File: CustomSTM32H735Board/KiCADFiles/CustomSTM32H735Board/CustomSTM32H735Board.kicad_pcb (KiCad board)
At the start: 2 copper layers, 4 parts, among them U1 STM32H735IGKx, U2 STM32H735IGTx

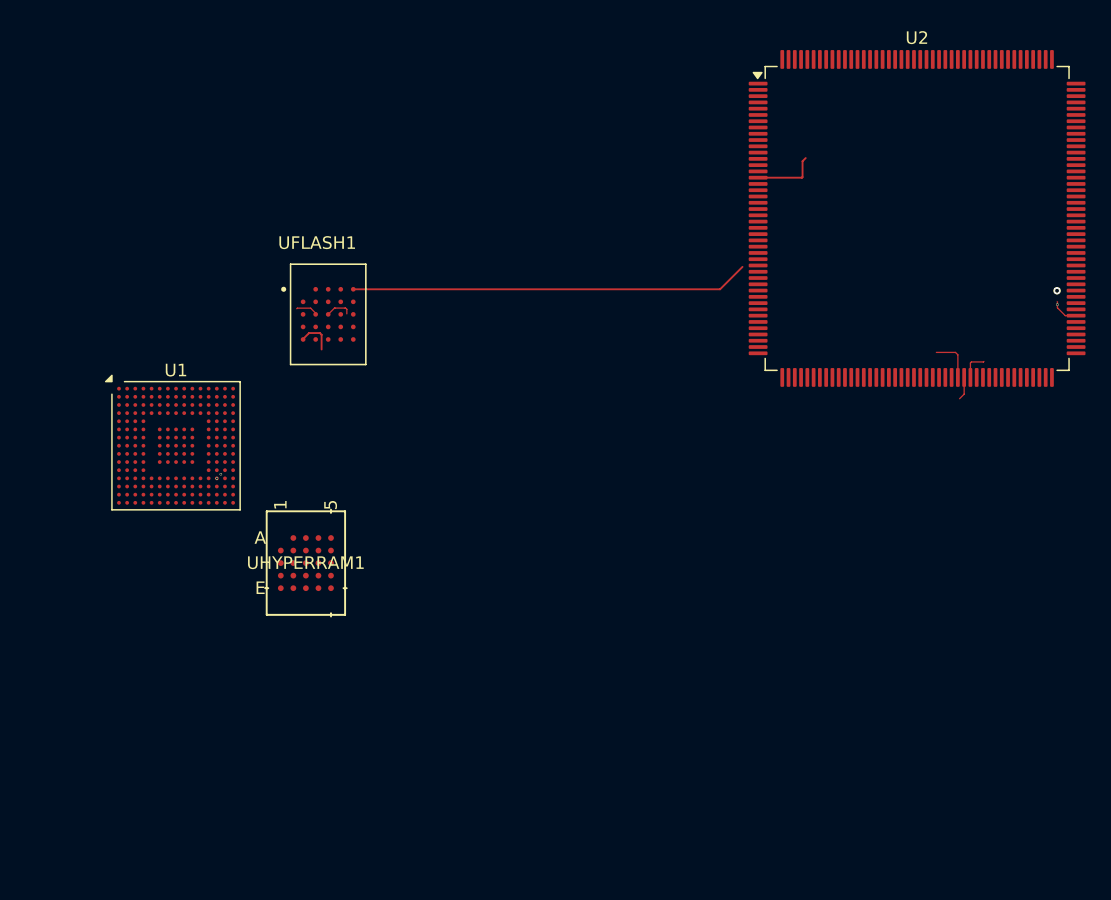
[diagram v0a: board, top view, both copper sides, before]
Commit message: started to assign LCD connector to STM32H735. Added NRST and Boot0 switch.
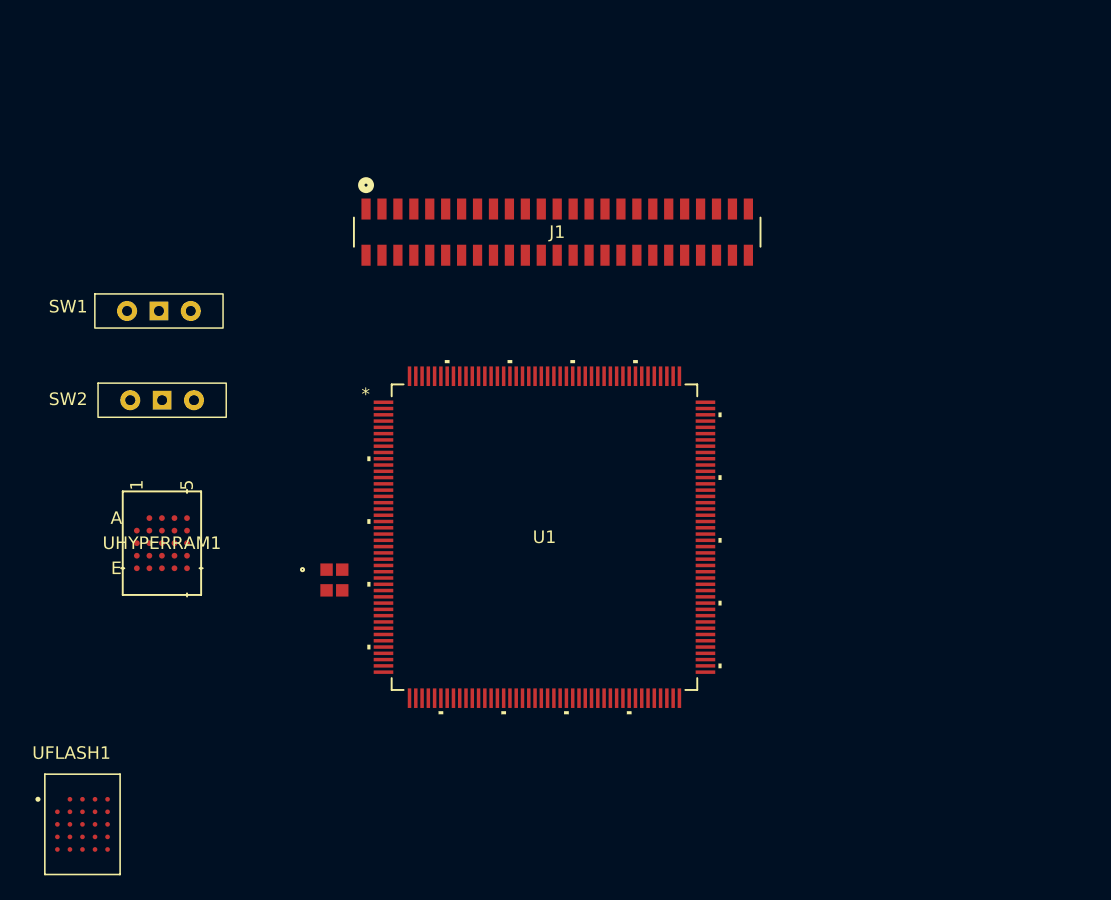
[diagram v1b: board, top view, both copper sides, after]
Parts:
- removed U2: STM32H735IGTx, Package_QFP:LQFP-176_24x24mm_P0.5mm
- added J1: FLE-125-01-G-DV, Private:CON50_2X25_UF_FLE_SAI, F.Cu at (125.5, 57.0)
- added SW1: SW_Wuerth_450301014042, Button_Switch_THT:SW_Slide-03_Wuerth-WS-SLTV_10x2.5x6.4_P2.54mm, F.Cu at (109.0, 61.5)
- added SW2: SW_Wuerth_450301014042, Button_Switch_THT:SW_Slide-03_Wuerth-WS-SLTV_10x2.5x6.4_P2.54mm, F.Cu at (109.2, 68.6)
- added X1: NSC5004A-25M, Private:NSC5004_NDK, F.Cu at (123.0, 82.9)
- U1: value STM32H735IGKx -> STM32H735IGT6; footprint Package_BGA:UFBGA-201_10x10mm_Layout15x15_P0.65mm -> Private:LQFP176_STM32H735IGT6_STM-M
- moved UFLASH1 45.1 mm to (102.9, 102.4)
- moved U1 30.3 mm to (139.7, 79.5)
- moved UHYPERRAM1 11.6 mm to (109.2, 80.0)
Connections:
- UFLASH1 pad B2: /PF10 -> /PB2
- UFLASH1 pad C3: /PB2 -> /PC5
- UFLASH1 pad D2: /PD12 -> /PF9
- UFLASH1 pad D3: /PD11 -> /PF8
- UFLASH1 pad D4: /PD13 -> /PA6
- UFLASH1 pad D5: /PD4 -> /PE7
- UFLASH1 pad E1: /PD7 -> /PE10
- UFLASH1 pad E2: /PG9 -> /PC3_C
- UFLASH1 pad E3: /PD5 -> /PC2_C
- UHYPERRAM1 pad B4: Net-(UHYPERRAM1-VCC) -> +3.3V
- UHYPERRAM1 pad D1: Net-(UHYPERRAM1-VCC) -> +3.3V
- UHYPERRAM1 pad E4: Net-(UHYPERRAM1-VCC) -> +3.3V
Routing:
- net /PG6: track 33.6 -> 0.00 mm
- net unconnected-(U2-VDDSMPS-Pad16): track 5.19 -> 0.00 mm
- net unconnected-(U2-PE11-Pad73): track 3.60 -> 0.00 mm
- net /PD7: track 2.94 -> 0.00 mm
- net unconnected-(U2-PD12-Pad95): track 2.47 -> 0.00 mm, vias 2 -> 0
- net unconnected-(U2-PE13-Pad75): track 2.28 -> 0.00 mm
- net /PB2: track 2.11 -> 0.00 mm
- net unconnected-(U2-PE12-Pad74): track 1.85 -> 0.00 mm
- net unconnected-(U1-PH11-PadM13): vias 1 -> 0
- net (no net): vias 2 -> 0

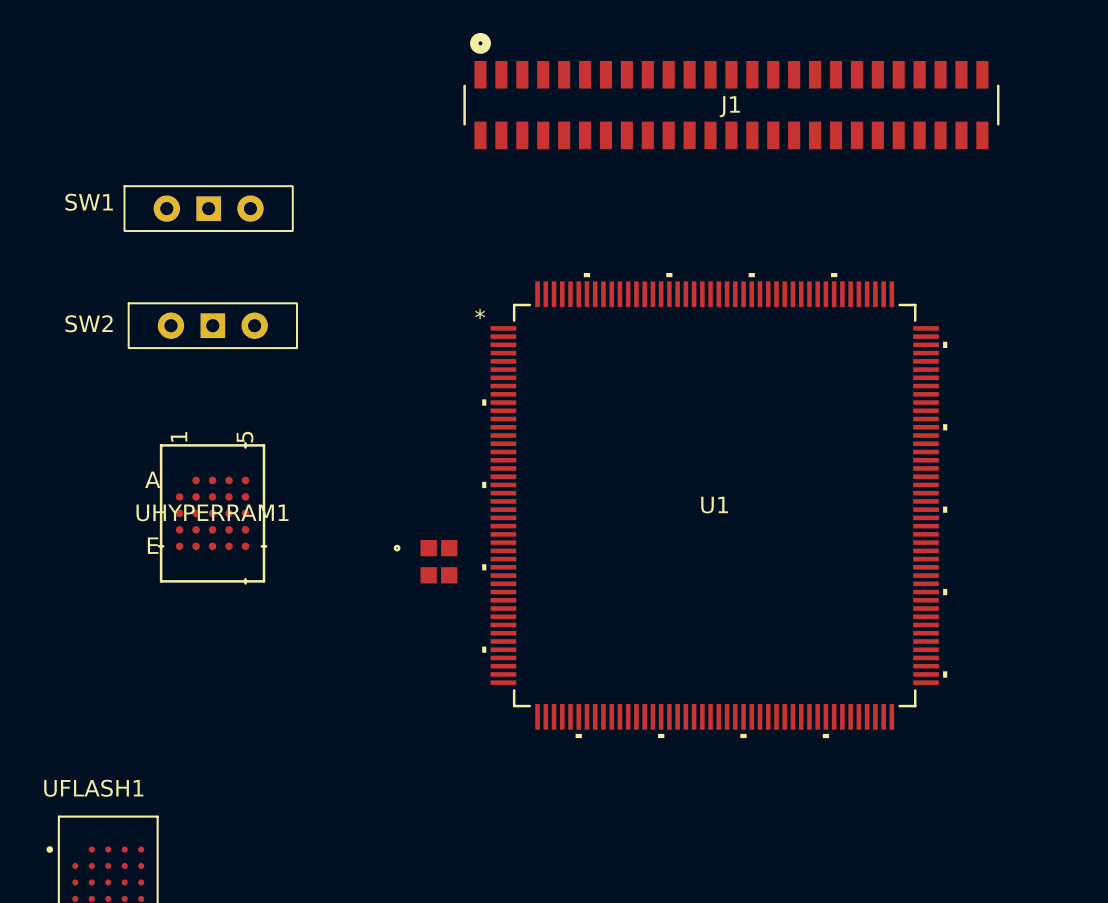
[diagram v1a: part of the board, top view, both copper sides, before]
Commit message: cleaned up repo by eliminating double STM32-DK files
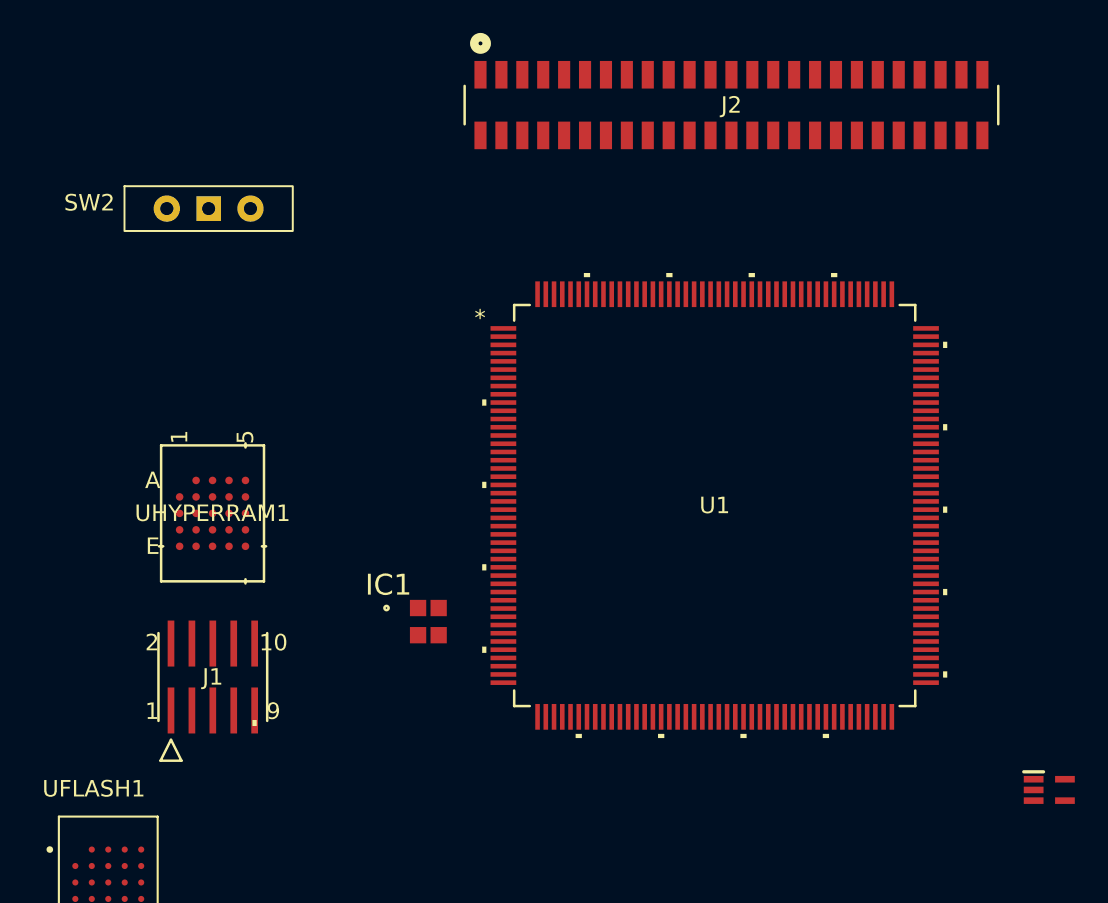
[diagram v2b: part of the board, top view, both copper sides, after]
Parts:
- removed the SW2 at (109.2, 68.6)
- added IC1: ESDALC6V1W5, Private:SOT65P210X110-5N, F.Cu at (160.0, 96.8)
- added J1: FTSH-105-01-L-DV-K, Private:CON10_2X5_DUK_FTSH_SAI-M, F.Cu at (109.2, 89.9)
- moved X1 3.69 mm to (122.3, 86.6)
- renumbered J1 to J2, SW1 to SW2
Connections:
- SW2 pad 1: Net-(SW1-B) -> Net-(SW2-B)
- SW2 pad 2: /VDD -> +3.3V
- SW2 pad 3: unconnected-(SW1-A-Pad3) -> Net-(SW2-A)
- U1 pad 104: unconnected-(U1B-PJ11-LTDC_G4-Pad104) -> /PJ11
- U1 pad 105: /VDD -> +3.3V
- U1 pad 113: /VDD -> +3.3V
- U1 pad 121: unconnected-(U1-Pad121) -> /VSS
- U1 pad 126: /VDD -> +3.3V
- U1 pad 13: /VDD -> +3.3V
- U1 pad 132: unconnected-(U1-Pad132) -> /PA13
- U1 pad 133: unconnected-(U1-Pad133) -> Net-(C11-Pad1)
- U1 pad 135: unconnected-(U1-Pad135) -> +3.3V
- U1 pad 136: /VDD -> +3.3V
- U1 pad 138: unconnected-(U1-Pad138) -> /PA14
- U1 pad 14: unconnected-(U1-Pad14) -> /VSS
- U1 pad 141: unconnected-(U1B-PC11-UART4_RX-Pad141) -> /PC11
- U1 pad 152: /VDD -> +3.3V
- U1 pad 16: unconnected-(U1-Pad16) -> /VSS
- U1 pad 160: /VDD -> +3.3V
- U1 pad 165: unconnected-(U1B-PB6-I2C1_SCL-Pad165) -> /PB6
- U1 pad 166: unconnected-(U1B-PB7-I2C1_SDA-Pad166) -> /PB7
- U1 pad 17: unconnected-(U1-Pad17) -> /VSS
- U1 pad 172: unconnected-(U1-Pad172) -> Net-(C12-Pad2)
- U1 pad 174: unconnected-(U1-Pad174) -> /PDR_ON
- U1 pad 175: unconnected-(U1-Pad175) -> +3.3V
- U1 pad 176: /VDD -> +3.3V
- U1 pad 25: /VDD -> +3.3V
- U1 pad 26: unconnected-(U1A-PF6-TIM23_CH1-Pad26) -> /PF6
- U1 pad 27: unconnected-(U1A-PF7-TIM23_CH2-Pad27) -> /PF7
- U1 pad 38: unconnected-(U1-Pad38) -> /VSS
- U1 pad 39: unconnected-(U1A-VREF+-VREFBUF_OUT-Pad39) -> Net-(SW2-A)
- U1 pad 40: Net-(SW1-B) -> Net-(L1-Pad2)
- U1 pad 41: unconnected-(U1A-PA0-UART4_TX-Pad41) -> /PA0
- U1 pad 44: /VDD -> +3.3V
- U1 pad 48: /VDD -> +3.3V
- U1 pad 49: unconnected-(U1A-PA4-DAC1_OUT1-Pad49) -> /PA4
- U1 pad 50: unconnected-(U1A-PA5-DAC1_OUT2-Pad50) -> /PA5
- U1 pad 52: unconnected-(U1A-PA7-LTDC_VSYNC-Pad52) -> /PA7
- U1 pad 53: unconnected-(U1A-PC4-LTDC_R7-Pad53) -> /PC4
- U1 pad 55: unconnected-(U1A-PB0-LTDC_R3-Pad55) -> /PB0
- U1 pad 56: unconnected-(U1A-PB1-LTDC_R6-Pad56) -> /PB1
- U1 pad 58: unconnected-(U1A-PF11-ADC1_INP2-Pad58) -> /PF11
- U1 pad 60: unconnected-(U1A-PF13-ADC2_INP2-Pad60) -> /PF13
- U1 pad 64: unconnected-(U1-Pad64) -> /VSS
- U1 pad 65: /VDD -> +3.3V
- U1 pad 7: /VDD -> +3.3V
- U1 pad 71: /VDD -> +3.3V
- U1 pad 78: unconnected-(U1A-PB10-I2C2_SCL-Pad78) -> /PB10
- U1 pad 79: unconnected-(U1A-PB11-I2C2_SDA-Pad79) -> /PB11
- U1 pad 8: unconnected-(U1-Pad8) -> +3.3V
- U1 pad 80: unconnected-(U1-Pad80) -> Net-(C10-Pad2)
- U1 pad 82: unconnected-(U1-Pad82) -> +3.3V
- U1 pad 84: /VDD -> +3.3V
- U1 pad 92: /VDD -> +3.3V
- U1 pad 99: /VDD -> +3.3V

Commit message: Work on layout and PCB of custom board. All connectors added. PCB size first draft.
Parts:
- removed IC1: ESDALC6V1W5, Private:SOT65P210X110-5N
- removed SW2: SW_Wuerth_450301014042, Button_Switch_THT:SW_Slide-03_Wuerth-WS-SLTV_10x2.5x6.4_P2.54mm
- added C10: 10uF, Capacitor_SMD:C_0805_2012Metric_Pad1.18x1.45mm_HandSolder, F.Cu at (27.7, 26.3)
- added C11: 10uF, Capacitor_SMD:C_0805_2012Metric_Pad1.18x1.45mm_HandSolder, F.Cu at (27.7, 29.3)
- added C12: 220pF, Capacitor_SMD:C_0805_2012Metric_Pad1.18x1.45mm_HandSolder, F.Cu at (32.5, 17.3)
- added C13: 4.7uF low ESR, Capacitor_SMD:C_0805_2012Metric_Pad1.18x1.45mm_HandSolder, F.Cu at (32.5, 20.3)
- added C14: 4.7uF low ESR, Capacitor_SMD:C_0805_2012Metric_Pad1.18x1.45mm_HandSolder, F.Cu at (32.5, 23.3)
- added C15: 4.7uF low ESR, Capacitor_SMD:C_0805_2012Metric_Pad1.18x1.45mm_HandSolder, F.Cu at (32.5, 26.3)
- added C2: 100nF, Capacitor_SMD:C_0805_2012Metric_Pad1.18x1.45mm_HandSolder, F.Cu at (22.8, 17.3)
- added C3: 100nF, Capacitor_SMD:C_0805_2012Metric_Pad1.18x1.45mm_HandSolder, F.Cu at (22.8, 20.3)
- added C4: 100nF, Capacitor_SMD:C_0805_2012Metric_Pad1.18x1.45mm_HandSolder, F.Cu at (22.8, 23.3)
- added C5: 100nF, Capacitor_SMD:C_0805_2012Metric_Pad1.18x1.45mm_HandSolder, F.Cu at (22.8, 26.3)
- added C6: 100nF, Capacitor_SMD:C_0805_2012Metric_Pad1.18x1.45mm_HandSolder, F.Cu at (22.8, 29.3)
- added C7: 100nF, Capacitor_SMD:C_0805_2012Metric_Pad1.18x1.45mm_HandSolder, F.Cu at (27.7, 17.3)
- added C8: 100nF, Capacitor_SMD:C_0805_2012Metric_Pad1.18x1.45mm_HandSolder, F.Cu at (27.7, 20.3)
- added C9: 100nF, Capacitor_SMD:C_0805_2012Metric_Pad1.18x1.45mm_HandSolder, F.Cu at (27.7, 23.3)
- added FB1: FBMJ1608, Inductor_SMD:L_0603_1608Metric_Pad1.05x0.95mm_HandSolder, F.Cu at (33.8, 32.1)
- added FB2: FCM1608, Inductor_SMD:L_0603_1608Metric_Pad1.05x0.95mm_HandSolder, F.Cu at (33.8, 34.6)
- added H1: MountingHole_Pad_MP, MountingHole:MountingHole_2.7mm_M2.5_Pad_TopBottom, F.Cu at (53.1, 53.1)
- added H2: MountingHole_Pad_MP, MountingHole:MountingHole_2.7mm_M2.5_Pad_TopBottom, F.Cu at (53.1, 127.0)
- added H3: MountingHole_Pad_MP, MountingHole:MountingHole_2.7mm_M2.5_Pad_TopBottom, F.Cu at (207.0, 53.0)
- added H4: MountingHole_Pad_MP, MountingHole:MountingHole_2.7mm_M2.5_Pad_TopBottom, F.Cu at (207.0, 127.0)
- added H5: MountingHole_Pad_MP, MountingHole:MountingHole_2.7mm_M2.5_Pad_TopBottom, F.Cu at (70.1, 62.0)
- added H6: MountingHole_Pad_MP, MountingHole:MountingHole_2.7mm_M2.5_Pad_TopBottom, F.Cu at (188.0, 62.0)
- added H7: MountingHole_Pad_MP, MountingHole:MountingHole_2.7mm_M2.5_Pad_TopBottom, F.Cu at (70.1, 117.9)
- added H8: MountingHole_Pad_MP, MountingHole:MountingHole_2.7mm_M2.5_Pad_TopBottom, F.Cu at (190.0, 117.9)
- added J1: Conn_01x03_Socket, Connector_JST:JST_XH_B2B-XH-AM_1x02_P2.50mm_Vertical, F.Cu at (252.1, 64.7)
- added J2: Conn_02x10_Odd_Even, Connector_IDC:IDC-Header_2x10_P2.54mm_Vertical, B.Cu at (79.2, 54.9)
- added JADC1: Conn_01x02_Socket, Connector_JST:JST_XH_B3B-XH-A_1x03_P2.50mm_Vertical, F.Cu at (240.1, 47.0)
- added JDAC1: Conn_01x03_Socket, Connector_JST:JST_XH_B3B-XH-A_1x03_P2.50mm_Vertical, F.Cu at (240.1, 54.8)
- added JI2C1: Conn_01x03_Socket, Connector_JST:JST_XH_B3B-XH-A_1x03_P2.50mm_Vertical, F.Cu at (240.1, 62.6)
- added JI2C2: Conn_01x03_Socket, Connector_JST:JST_XH_B3B-XH-A_1x03_P2.50mm_Vertical, F.Cu at (240.1, 70.4)
- added JI2C3: Conn_01x03_Socket, Connector_JST:JST_XH_B3B-XH-A_1x03_P2.50mm_Vertical, F.Cu at (240.1, 78.2)
- added JP1: SolderJumper_3_Open, Jumper:SolderJumper-3_P1.3mm_Open_Pad1.0x1.5mm_NumberLabels, F.Cu at (34.5, 37.6)
- added JUART1: Conn_01x03_Socket, Connector_JST:JST_XH_B3B-XH-A_1x03_P2.50mm_Vertical, F.Cu at (240.1, 86.0)
- added L1: 2.2uH, Inductor_SMD:L_Murata_DFE201610P, F.Cu at (113.8, 87.6)
- added R1: 10k, Resistor_SMD:R_0805_2012Metric_Pad1.20x1.40mm_HandSolder, F.Cu at (18.1, 17.3)
- added R10: 5k1, Resistor_SMD:R_0805_2012Metric_Pad1.20x1.40mm_HandSolder, F.Cu at (18.1, 26.1)
- added R11: R, Resistor_SMD:R_0805_2012Metric_Pad1.20x1.40mm_HandSolder, F.Cu at (18.1, 29.1)
- added R12: 22R, Resistor_SMD:R_0805_2012Metric_Pad1.20x1.40mm_HandSolder, F.Cu at (18.1, 32.0)
- added R13: 22R, Resistor_SMD:R_0805_2012Metric_Pad1.20x1.40mm_HandSolder, F.Cu at (18.1, 35.0)
- added R14: 22R, Resistor_SMD:R_0805_2012Metric_Pad1.20x1.40mm_HandSolder, F.Cu at (18.1, 37.9)
- added R2: 10k, Resistor_SMD:R_0805_2012Metric_Pad1.20x1.40mm_HandSolder, F.Cu at (18.1, 20.2)
- added R3: 10k, Resistor_SMD:R_0805_2012Metric_Pad1.20x1.40mm_HandSolder, F.Cu at (18.1, 23.2)
- added R4: 4.7k, Resistor_SMD:R_0805_2012Metric_Pad1.20x1.40mm_HandSolder, F.Cu at (251.0, 45.1)
- added R5: 4.7k, Resistor_SMD:R_0805_2012Metric_Pad1.20x1.40mm_HandSolder, F.Cu at (251.0, 48.1)
- added R6: 4.7k, Resistor_SMD:R_0805_2012Metric_Pad1.20x1.40mm_HandSolder, F.Cu at (251.0, 51.0)
- added R7: 4.7k, Resistor_SMD:R_0805_2012Metric_Pad1.20x1.40mm_HandSolder, F.Cu at (251.0, 54.0)
- added R8: 4.7k, Resistor_SMD:R_0805_2012Metric_Pad1.20x1.40mm_HandSolder, F.Cu at (251.0, 56.9)
- added R9: 4.7k, Resistor_SMD:R_0805_2012Metric_Pad1.20x1.40mm_HandSolder, F.Cu at (251.0, 59.9)
- added SW1: SW_Omron_B3FS, Button_Switch_SMD:SW_SPST_Omron_B3FS-100xP, F.Cu at (56.6, 61.0)
- added TP1: TestPoint, Connector_Pin:Pin_D0.7mm_L6.5mm_W1.8mm_FlatFork, F.Cu at (110.2, 88.4)
- J4: renamed from J2; moved to B.Cu
- UHYPERRAM1: moved to B.Cu
- moved J3 54.2 mm to (55.4, 83.8)
- moved X1 46.7 mm to (162.8, 109.7)
- moved UHYPERRAM1 22.0 mm to (125.7, 94.5), turned to 180 degrees
- moved U1 14.5 mm to (130.4, 90.6)
- moved J4 11.4 mm to (114.1, 56.3)
- moved UFLASH1 7.62 mm to (110.2, 104.4), turned to 180 degrees
- renumbered J1 to J3
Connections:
- U1 pad 100: /VSS -> GND
- U1 pad 106: /VSS -> GND
- U1 pad 112: /VSS -> GND
- U1 pad 119: /VSS -> GND
- U1 pad 12: /VSS -> GND
- U1 pad 121: /VSS -> GND
- U1 pad 127: unconnected-(U1-Pad127) -> /PA8
- U1 pad 133: Net-(C11-Pad1) -> /VDD_SDC
- U1 pad 134: /VSS -> GND
- U1 pad 135: +3.3V -> /VDD_SDC
- U1 pad 137: /VSS -> GND
- U1 pad 14: /VSS -> /VSSSMPS
- U1 pad 15: unconnected-(U1-Pad15) -> /VLXSMPS
- U1 pad 151: /VSS -> GND
- U1 pad 159: /VSS -> GND
- U1 pad 16: /VSS -> /VDDSMPS
- U1 pad 17: /VSS -> /VDD_SDC
- U1 pad 172: Net-(C12-Pad2) -> /VDD_SDC
- U1 pad 173: /VSS -> GND
- U1 pad 175: +3.3V -> /VDD_SDC
- U1 pad 24: /VSS -> GND
- U1 pad 38: /VSS -> GND
- U1 pad 45: /VSS -> GND
- U1 pad 47: /VSS -> GND
- U1 pad 6: /VSS -> GND
- U1 pad 64: /VSS -> GND
- U1 pad 70: /VSS -> GND
- U1 pad 80: Net-(C10-Pad2) -> /VDD_SDC
- U1 pad 81: /VSS -> GND
- U1 pad 82: +3.3V -> /VDD_SDC
- U1 pad 83: /VSS -> GND
- U1 pad 93: /VSS -> GND
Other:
- board outline added: 160 x 80 mm
